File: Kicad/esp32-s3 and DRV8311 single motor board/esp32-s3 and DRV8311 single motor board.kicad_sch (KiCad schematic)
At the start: 57 parts, among them J1 JST SH SM04B, J2 7 pin FPC 0.3mm, SW1 SW_Push, SW2 SW_Push, U5 ESP32-S3, U6 74HC595, Y1 40mhz, 10ppm

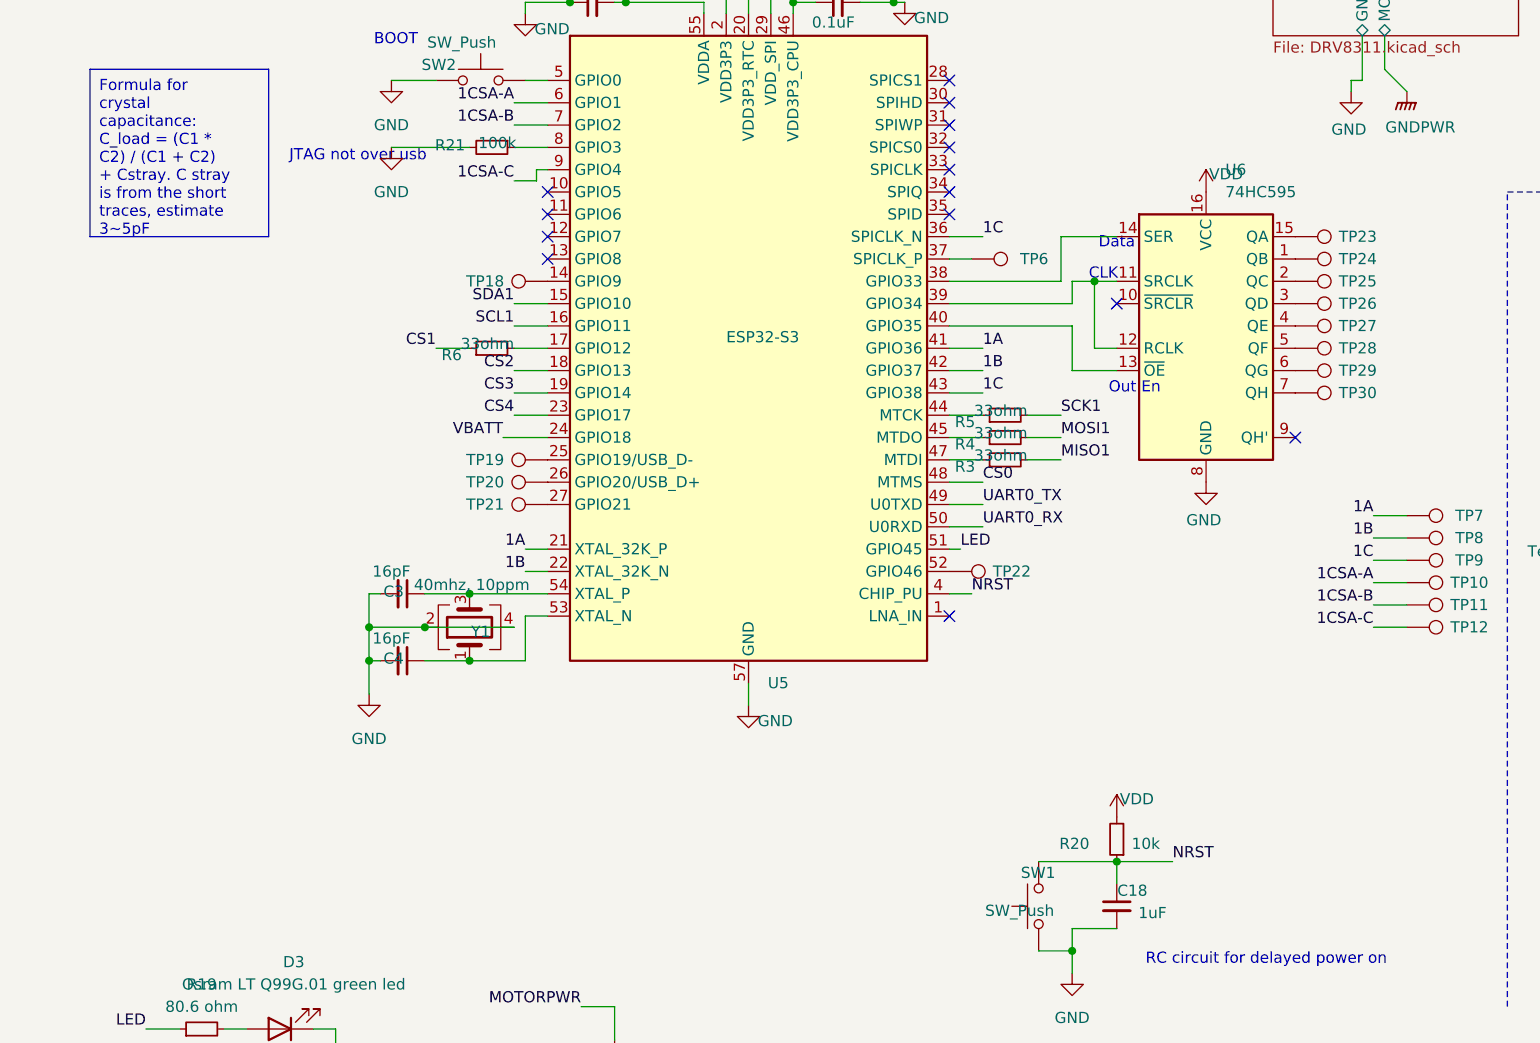
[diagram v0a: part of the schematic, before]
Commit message: Switched Shift register lines to USB
The shift register will be virtually unaffected by any USB activity, and the usb lines should not be affected at low speeds for having a shift register on the bus. In my final design I will be using every last pin, so I need to use the USB lines for something. This seemed like the most logical choice, since outputs have a dedicated enable line. I can disable USB entirely as well and just program over JTAG/ encoder SPI bus.
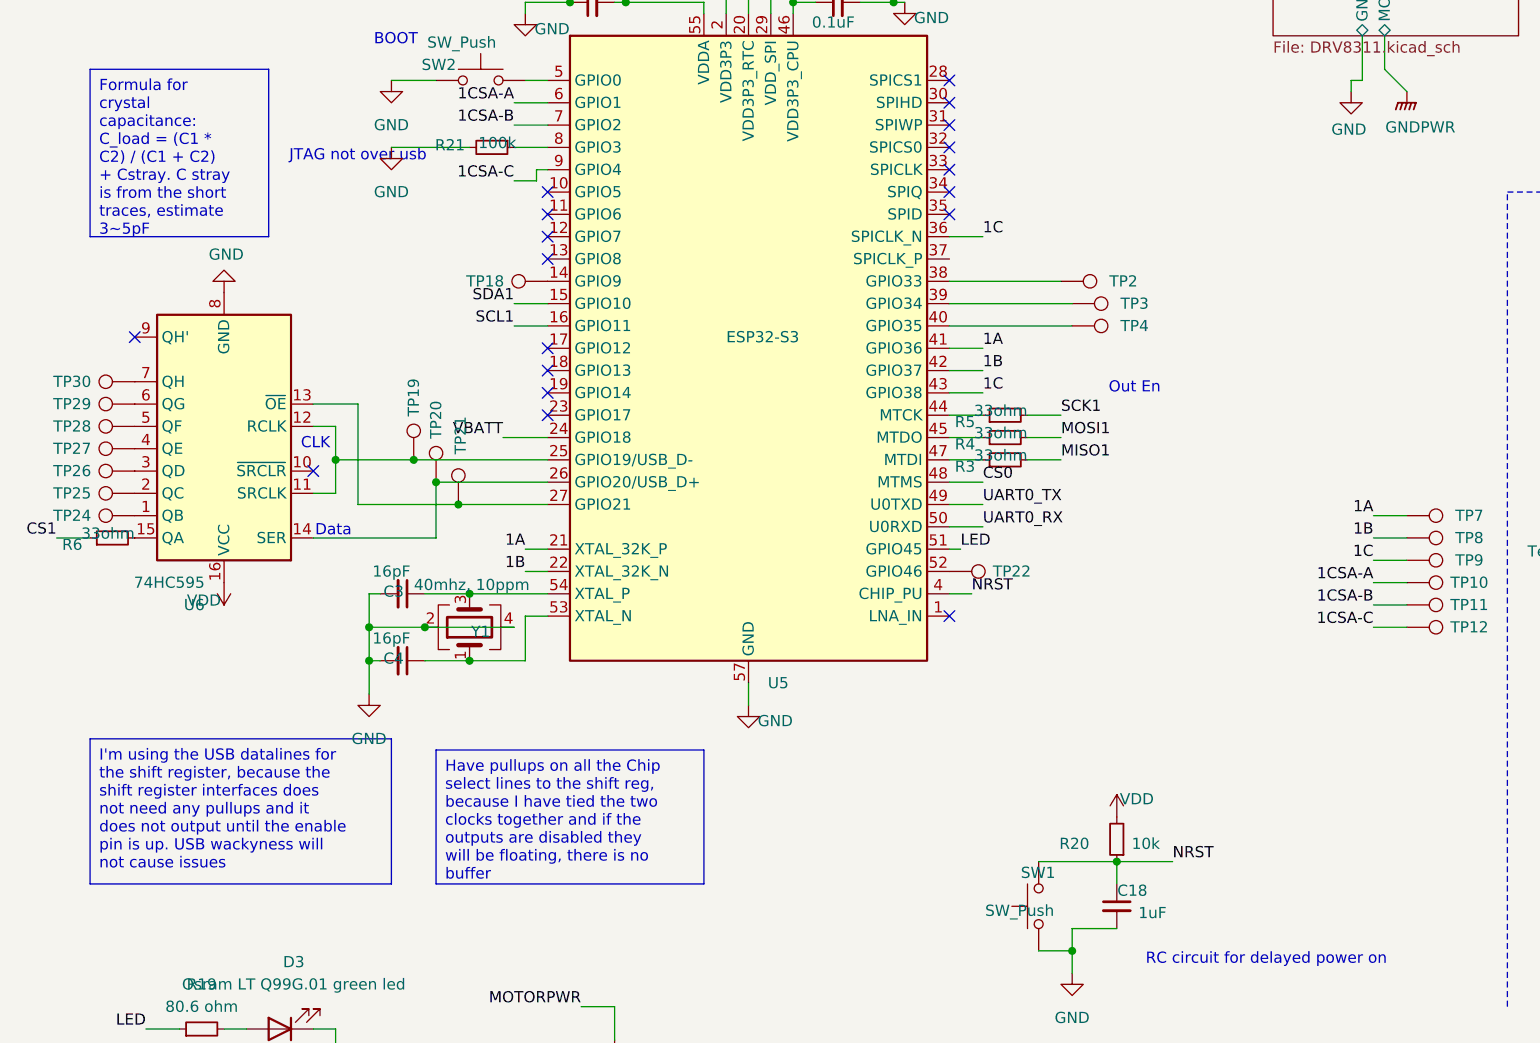
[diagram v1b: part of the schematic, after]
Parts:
- removed TP23, TP6: ~, TestPoint:TestPoint_Pad_D1.0mm, symbol Connector:TestPoint
- added TP2, TP3, TP4: ~, TestPoint:TestPoint_Pad_D1.0mm, symbol Connector:TestPoint
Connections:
- net at TP20.1, U5.26 (GPIO20/USB_D+): now also U6.14 (SER)
- net at TP21.1, U5.27 (GPIO21): now also U6.13 (~{OE})
- net at TP19.1, U5.25 (GPIO19/USB_D-): now also U6.11 (SRCLK), U6.12 (RCLK)
- net at R6.2: now also U6.15 (QA); no longer U5.17 (GPIO12)
- net at U5.38 (GPIO33): now also TP2.1; no longer U6.14 (SER)
- net at U5.40 (GPIO35): now also TP4.1; no longer U6.13 (~{OE})
- net CS2: no longer names the net of U5.18 (GPIO13)
- net CS3: no longer names the net of U5.19 (GPIO14)
- net CS4: no longer names the net of U5.23 (GPIO17)
- new net: TP3.1, U5.39 (GPIO34)
- no-connect marks 16 -> 20
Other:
- moved on the sheet: R6, TP19, TP20, TP21, TP24, TP25, TP26, TP27, TP28, TP29, TP30, U6
